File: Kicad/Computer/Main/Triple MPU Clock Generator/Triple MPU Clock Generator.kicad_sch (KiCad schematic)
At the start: 45 parts, among them IC1 AP7365-33WG-7, IC10 74LVC74APW,118, IC11 74LVC157APW,118, IC12 74LVC1G08GV,125, IC13 74LVC14APW,118, IC2 74LVC74APW,118, IC3 74LVC74APW,118, IC4 74LVC74APW,118, IC5 74LVC74APW,118, IC6 74LVC74APW,118, IC7 74LVC157APW,118, IC8 DS1813R-10+T&R, IC9 74LVC125APW-Q100J, J1 Conn_02x32_Counter_Clockwise, J10 Pin_Header_01x32, J11 Pin_Header_01x32, J2 Conn_01x03_Socket, J3 Conn_01x03_Socket, J4 Conn_01x03_Socket, J5 Conn_01x03_Socket, J6 Conn_01x03_Socket, J7 Conn_01x03_Socket, J8 Conn_01x03_Socket, J9 Conn_01x03_Socket

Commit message: Re-worked Dual Clock Generator.
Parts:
- removed IC9: 74LVC125APW-Q100J, SOP65P640X110-14N, symbol Nexperia:74LVC125APW-Q100J
- removed J2, J3, J4, J5, J6, J7, J8, J9: Conn_01x03_Socket, Connector_PinSocket_2.54mm:PinSocket_1x03_P2.54mm_Vertical, symbol Connector:Conn_01x03_Socket
- removed NT1: NetTie_2, NetTie:NetTie-2_SMD_Pad0.5mm, symbol Device:NetTie_2
- removed R1: 4.7KΩ, SamacSys_Parts:R_0805, symbol HCP65:R_0805
- removed RN1: CAY16-471J4LF, CAY16-J4, symbol Bourns:CAY16-471J4LF
- removed RN2: CAY16-151J4LF, SamacSys_Parts:CAY16-J4, symbol Bourns:CAY16-151J4LF
- removed S1: NDS-04-V, NDS04V, symbol Apem:NDS-04-V
- added CN1, CN2, CN3, CN4, CN5, CN6: CA0612KRX7R9BB100, SamacSys_Parts:CA0612KRX7R9BB100, symbol Yageo:CA0612KRX7R9BB100
- added J4, J5: Conn_01x04_Socket, Connector_PinSocket_2.54mm:PinSocket_1x04_P2.54mm_Vertical, symbol Connector:Conn_01x04_Socket
- added RN1, RN6, RN7, RN8, RN9: CAY16-200J4LF, CAY-16-F4, symbol Bourns:CAY16-200J4LF
- added RN3: CAY16-100J4LF, CAY-16-F4, symbol Bourns:CAY16-100J4LF
- R2: value 3.3KΩ -> 4.7KΩ
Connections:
- net 3.3V: now also J5.1 (Pin_1)
- net CK_{0}: now also RN8.1 (R1); no longer IC11.2 (1I0), IC4.12 (2D)
- net CK_{1}: now also RN9.1 (R1); no longer IC11.3 (1I1), IC5.12 (2D)
- net CK_{2}: now also RN8.2 (R2); no longer IC11.5 (2I0), IC6.12 (2D)
- net CK_{3}: now also RN9.2 (R2); no longer IC10.12 (2D), IC11.6 (2I1)
- net CK_{4}: now also RN8.3 (R3); no longer IC11.11 (3I0), IC2.12 (2D)
- net CK_{5}: now also RN9.3 (R3); no longer IC11.10 (3I1), IC3.12 (2D)
- net CLK: now also IC13.9 (4A), J5.3 (Pin_3); no longer IC12.2 (A)
- net GND: now also CN1.5, CN1.6, CN1.7, CN1.8, CN2.5, CN2.6, CN2.7, CN2.8, CN3.5, CN3.6, CN3.7, CN3.8, CN4.5, CN4.6, CN4.7, CN4.8, CN5.5, CN5.6, CN5.7, CN5.8, CN6.5, CN6.6, CN6.7, CN6.8, J4.3 (Pin_3); no longer IC13.13 (6A), IC13.9 (4A)
- net MA_{0}: now also RN6.2 (R2); no longer IC4.2 (1D), IC7.2 (1I0)
- net MA_{1}: now also RN7.2 (R2); no longer IC5.2 (1D), IC7.3 (1I1)
- net MA_{2}: now also RN6.3 (R3); no longer IC6.2 (1D), IC7.5 (2I0)
- net MA_{3}: now also RN7.3 (R3); no longer IC10.2 (1D), IC7.6 (2I1)
- net MA_{4}: now also RN6.4 (R4); no longer IC2.2 (1D), IC7.11 (3I0)
- net MA_{5}: now also RN7.4 (R4); no longer IC3.2 (1D), IC7.10 (3I1)
- net Reset: now also RN7.1 (R1); no longer IC13.3 (2A)
- net ~{Q}_{0}: now also RN8.4 (R4); no longer J1.11 (Pin_11)
- net ~{Q}_{1}: now also RN9.4 (R4); no longer J1.54 (Pin_54)
- net ~{Q}_{2}: now also RN1.4 (R4); no longer J1.44 (Pin_44)
- net ~{Reset}_{OUT}: now also IC13.12 (6Y)
- net ~{Y0}: now also RN1.1 (R1); no longer J1.13 (Pin_13)
- net ~{Y1}: now also RN1.2 (R2); no longer J1.52 (Pin_52)
- net ~{Y2}: now also RN1.3 (R3); no longer J1.46 (Pin_46)
- net ~{CLK}: now reaches IC13.8 (4Y)
- net ~{CLK}: now also RN3.2 (R2)
- net !(~{RST}⋅CLK) renamed !(R⋅CLK)_{s}
- net !(R⋅CLK)_{s}: now also CN1.3, RN3.6 (R3); no longer IC13.6 (3Y)
- net ~{RST} renamed ~{Reset}_{2s}
- net ~{Reset}_{2s}: now also IC13.13 (6A), CN2.1, J4.1 (Pin_1), RN6.8 (R1); no longer IC13.4 (2Y)
- net ~{RST}⋅CLK renamed R⋅CLK_{s}
- net R⋅CLK_{s}: now also CN1.4, RN3.5 (R4); no longer IC12.4 (Y)
- new net: CN1.1, RN3.8 (R1)
- new net !(R⋅CLK): IC13.6 (3Y), RN3.3 (R3)
- new net CK_{0s}: CN4.1, IC11.2 (1I0), IC4.12 (2D), RN8.8 (R1)
- new net CK_{1s}: CN5.1, IC11.3 (1I1), IC5.12 (2D), RN9.8 (R1)
- new net CK_{2s}: CN4.2, IC11.5 (2I0), IC6.12 (2D), RN8.7 (R2)
- new net CK_{3s}: CN5.2, IC10.12 (2D), IC11.6 (2I1), RN9.7 (R2)
- new net CK_{4s}: CN4.3, IC11.11 (3I0), IC2.12 (2D), RN8.6 (R3)
- new net CK_{5s}: CN5.3, IC11.10 (3I1), IC3.12 (2D), RN9.6 (R3)
- new net MA_{0s}: CN2.2, IC4.2 (1D), IC7.2 (1I0), RN6.7 (R2)
- new net MA_{1s}: CN3.2, IC5.2 (1D), IC7.3 (1I1), RN7.7 (R2)
- new net MA_{2s}: CN2.3, IC6.2 (1D), IC7.5 (2I0), RN6.6 (R3)
- new net MA_{3s}: CN3.3, IC10.2 (1D), IC7.6 (2I1), RN7.6 (R3)
- new net MA_{4s}: CN2.4, IC2.2 (1D), IC7.11 (3I0), RN6.5 (R4)
- new net MA_{5s}: CN3.4, IC3.2 (1D), IC7.10 (3I1), RN7.5 (R4)
- new net Reset_{s}: CN3.1, IC13.3 (2A), RN7.8 (R1)
- new net R⋅CLK: IC12.4 (Y), RN3.4 (R4)
- new net ~{CLK}_{s}: CN1.2, IC12.2 (A), RN3.7 (R2)
- new net ~{Q}_{0s}: CN4.4, J1.11 (Pin_11), RN8.5 (R4)
- new net ~{Q}_{1s}: CN5.4, J1.54 (Pin_54), RN9.5 (R4)
- new net ~{Q}_{2s}: CN6.4, J1.44 (Pin_44), RN1.5 (R4)
- new net ~{Reset}_{2}: IC13.4 (2Y), RN6.1 (R1)
- new net ~{Y0}_{s}: CN6.1, J1.13 (Pin_13), RN1.8 (R1)
- new net ~{Y1}_{s}: CN6.2, J1.52 (Pin_52), RN1.7 (R2)
- new net ~{Y2}_{s}: CN6.3, J1.46 (Pin_46), RN1.6 (R3)
- no-connect marks 69 -> 64

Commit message: Moved clock generator pins.
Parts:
- removed J1: Conn_02x32_Counter_Clockwise, SamacSys_Parts:DIP-64_Board_W22.86mm, symbol Connector_Generic:Conn_02x32_Counter_Clockwise
- added CN7, CN8: CA0612KRX7R9BB100, SamacSys_Parts:CA0612KRX7R9BB100, symbol Yageo:CA0612KRX7R9BB100
- added J2: Conn_02x32_Counter_Clockwise, SamacSys_Parts:DIP-64_Board_W22.86mm, symbol Connector_Generic:Conn_02x32_Counter_Clockwise
- added RN2, RN4: CAY16-200J4LF, CAY-16-F4, symbol Bourns:CAY16-200J4LF
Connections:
- net 3.3V: now also J5.2 (Pin_2), J2.61 (Pin_61); no longer J5.1 (Pin_1)
- net 5V: now also J4.1 (Pin_1), J2.3 (Pin_3), J2.35 (Pin_35)
- net CLK: now also J5.4 (Pin_4), J2.59 (Pin_59); no longer J5.3 (Pin_3)
- net GND: now also J4.4 (Pin_4), CN7.6, CN7.7, CN7.8, CN8.6, CN8.7, CN8.8, J2.10 (Pin_10), J2.23 (Pin_23), J2.42 (Pin_42), J2.55 (Pin_55), J2.6 (Pin_6); no longer CN1.8, CN3.8, IC13.11 (5A), J4.3 (Pin_3)
- net Reset: now also IC13.3 (2A); no longer RN7.1 (R1)
- net R⋅CLK: now also IC13.5 (3A)
- net R⋅CLK_{s}: no longer IC13.5 (3A)
- net ~{Q}_{0}: now also CN8.1, J2.11 (Pin_11), RN4.4 (R4); no longer IC11.4 (1Y)
- net ~{Q}_{1}: now also CN8.2, J2.14 (Pin_14), RN4.3 (R3); no longer IC11.7 (2Y)
- net ~{Q}_{2}: now also CN8.3, J2.17 (Pin_17), RN4.2 (R2); no longer IC11.9 (3Y)
- net ~{Reset}: now also J2.13 (Pin_13)
- net ~{Reset}_{2s}: now also IC13.11 (5A), J4.2 (Pin_2), J2.4 (Pin_4); no longer IC13.13 (6A), J4.1 (Pin_1)
- net ~{Reset}_{OUT}: now also J2.9 (Pin_9)
- net ~{Y0}: now also CN7.1, J2.12 (Pin_12), RN2.4 (R4); no longer IC7.4 (1Y)
- net ~{Y1}: now also CN7.2, J2.15 (Pin_15), RN2.3 (R3); no longer IC7.7 (2Y)
- net ~{Y2}: now also CN7.3, J2.18 (Pin_18), RN2.2 (R2); no longer IC7.9 (3Y)
- net Reset_{2}: now reaches IC13.10 (5Y)
- net Reset_{2}: now also IC13.13 (6A)
- net Reset_{s}: no longer names the net of CN3.1, RN7.8 (R1)
- net Reset_{s}: no longer IC13.3 (2A)
- new net: IC11.4 (1Y), RN4.5 (R4)
- new net: IC11.7 (2Y), RN4.6 (R3)
- new net: IC11.9 (3Y), RN4.7 (R2)
- new net: CN7.4, RN2.1 (R1)
- new net: IC7.4 (1Y), RN2.5 (R4)
- new net: IC7.7 (2Y), RN2.6 (R3)
- new net: IC7.9 (3Y), RN2.7 (R2)
- new net: CN8.4, RN4.1 (R1)
- new net ~{Q}_{3}: J2.20 (Pin_20)
- new net ~{Y3}: J2.21 (Pin_21)
- no-connect marks 64 -> 72
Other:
- note added: "(CLK_{0})"
- note added: "(CLK_{1})"
- note added: "(CLK_{2})"
- note added: "(CLK_{3})"
- note added: "(Main Access_{0})"
- note added: "(Main Access_{1})"
- note added: "(Main Access_{2})"
- note added: "(Main Access_{3})"
- note added: "(~{Reset} CLK)"
- note added: "(~{Reset} Switch)"
- moved on the sheet: IC8, J4, J5, R2, S2

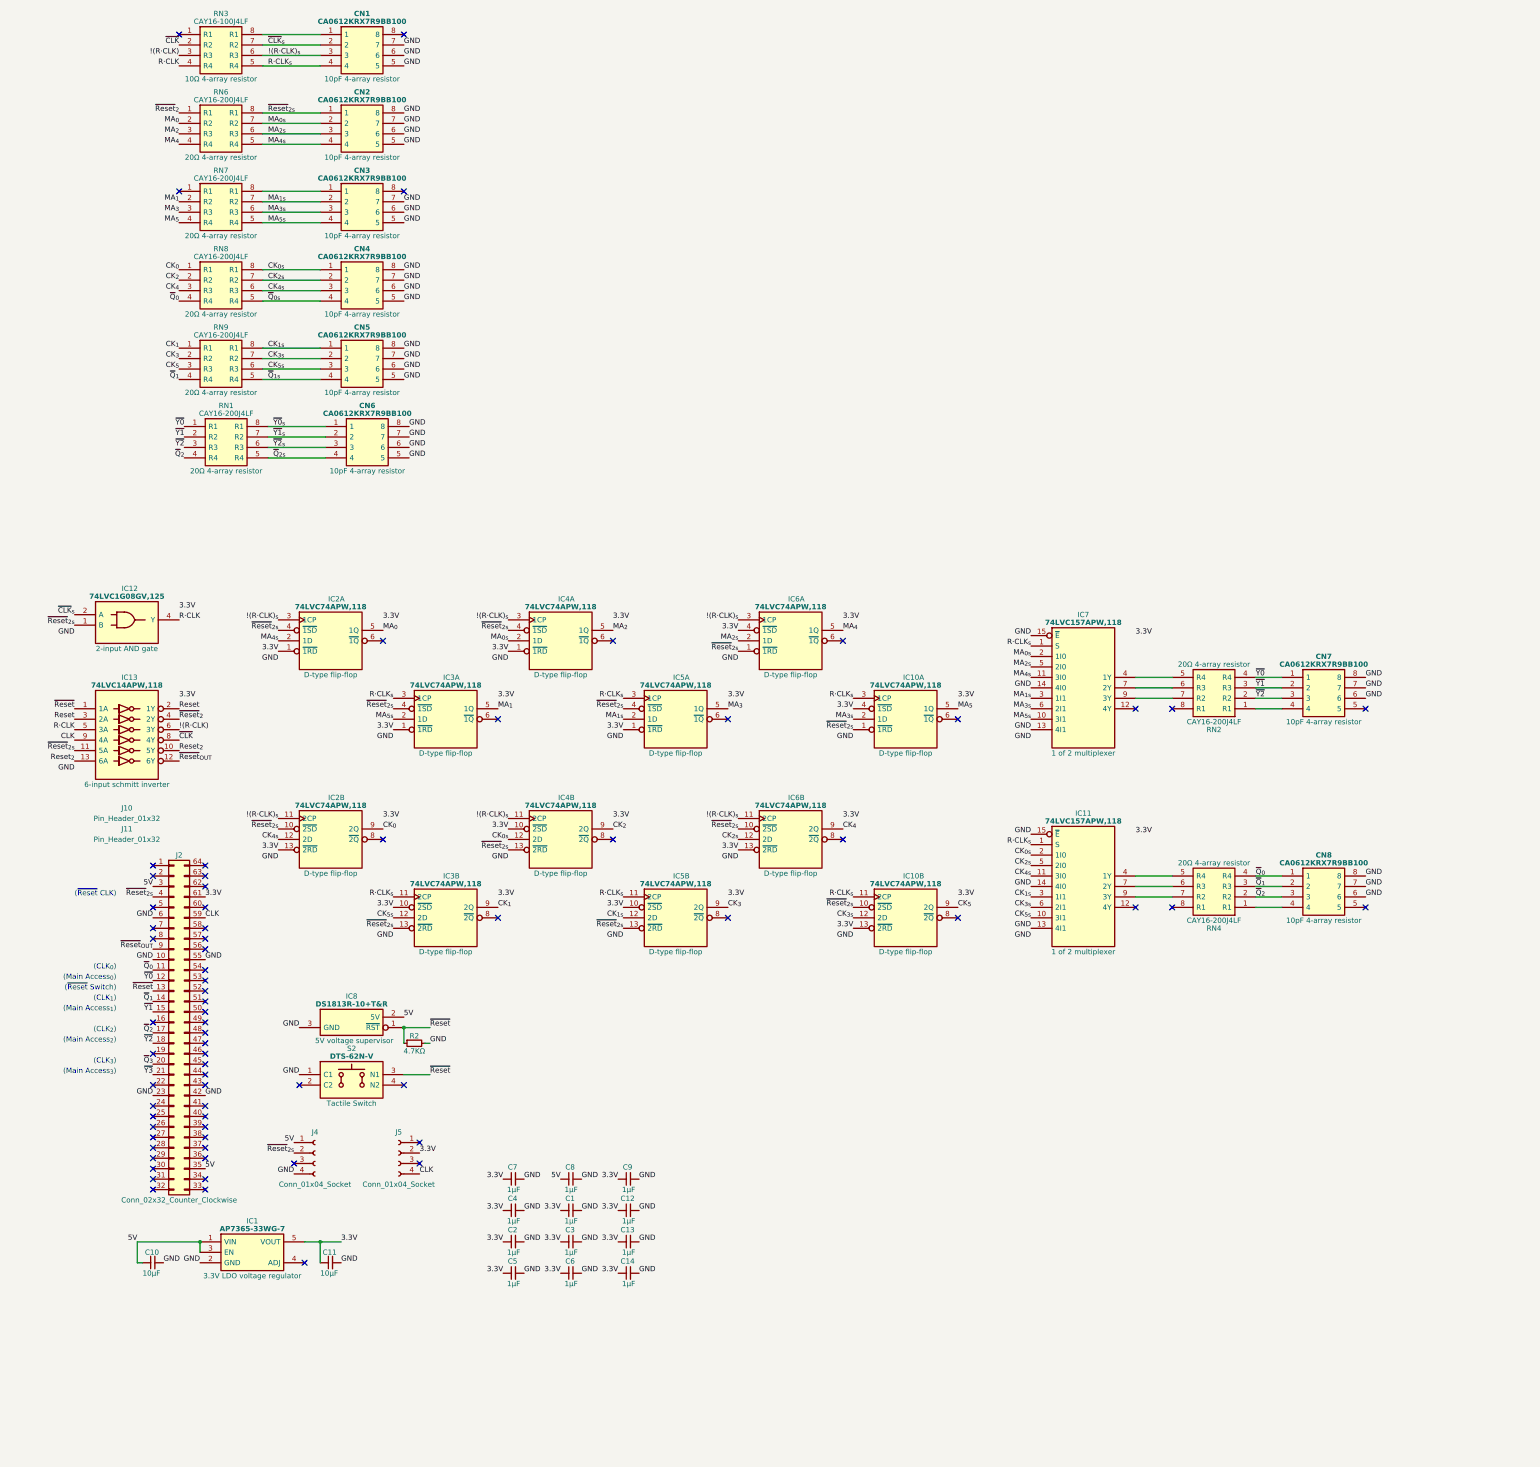
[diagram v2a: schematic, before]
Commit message: Routed Triple MPU Clock board.
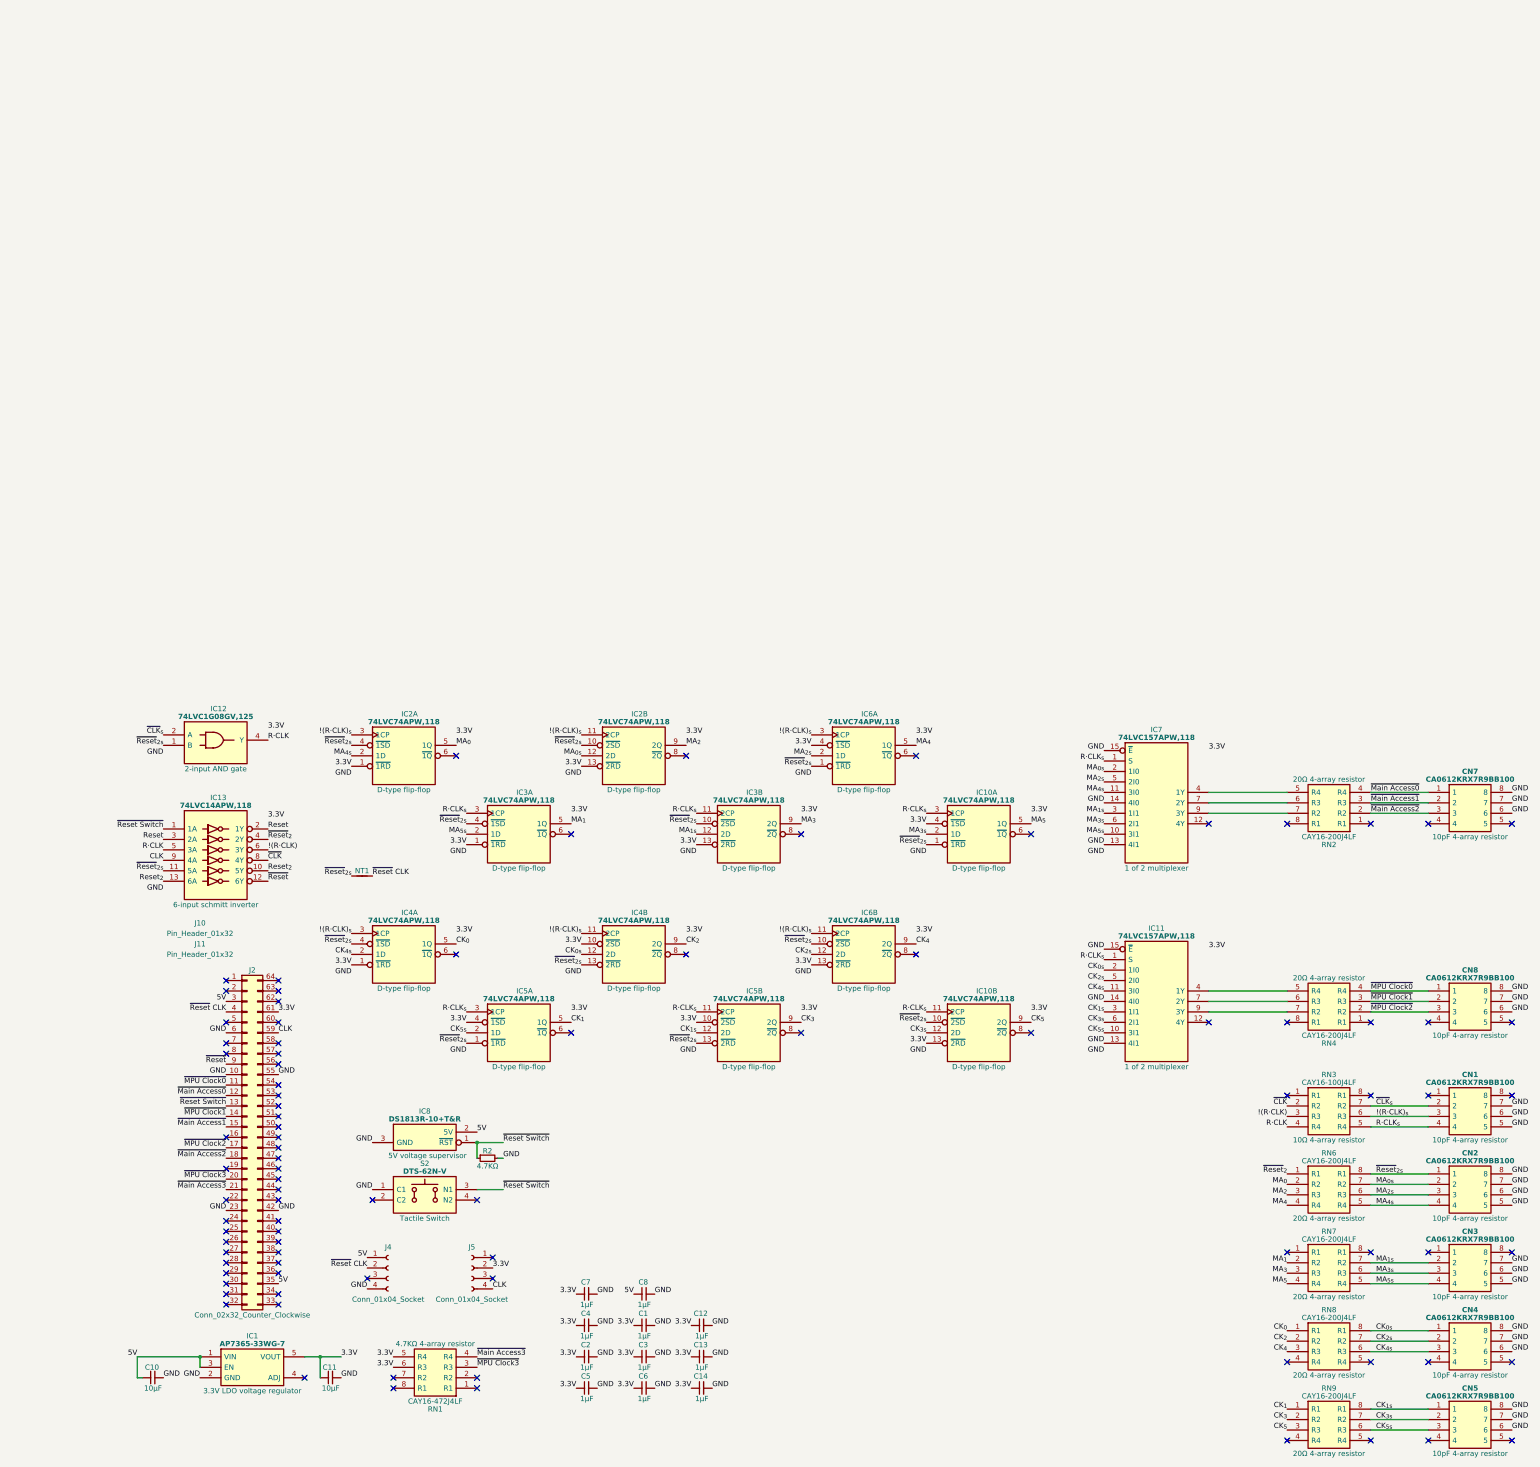
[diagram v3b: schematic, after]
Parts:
- removed C9: 1μF, SamacSys_Parts:C_0805, symbol HCP65:C_0805
- removed CN6: CA0612KRX7R9BB100, SamacSys_Parts:CA0612KRX7R9BB100, symbol Yageo:CA0612KRX7R9BB100
- removed RN1: CAY16-200J4LF, CAY-16-F4, symbol Bourns:CAY16-200J4LF
- added NT1: NetTie, NetTie:NetTie-2_SMD_Pad0.5mm, symbol HCP65:NetTie
- added RN1: CAY16-472J4LF, SamacSys_Parts:CAY16-F4, symbol Bourns:CAY16-472J4LF
- RN2, RN3, RN4, RN6, RN7, RN8, RN9: footprint CAY-16-F4 -> SamacSys_Parts:CAY16-F4
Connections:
- net ~{Reset}_{OUT} is gone; now on net ~{Reset}: IC13.12 (6Y), J2.9 (Pin_9)
- net 3.3V: now also IC3.13 (~{2RD}), IC5.4 (~{1SD}), RN1.5 (R4), RN1.6 (R3); no longer IC3.10 (~{2SD}), IC5.1 (~{1RD})
- net CK_{0}: now also IC4.5 (1Q); no longer IC2.9 (2Q)
- net CK_{1}: now also IC5.5 (1Q); no longer IC3.9 (2Q)
- net CK_{4s}: now also IC4.2 (1D); no longer IC2.12 (2D)
- net CK_{5s}: now also IC5.2 (1D); no longer IC3.12 (2D)
- net GND: no longer CN4.5, CN5.5
- net MA_{0s}: now also IC2.12 (2D); no longer IC4.2 (1D)
- net MA_{1s}: now also IC3.12 (2D); no longer IC5.2 (1D)
- net MA_{2}: now also IC2.9 (2Q); no longer IC4.5 (1Q)
- net MA_{3}: now also IC3.9 (2Q); no longer IC5.5 (1Q)
- net ~{Reset}: no longer IC13.1 (1A), IC8.1 (~{RST}), J2.13 (Pin_13), R2.1, S2.3 (N1)
- net ~{Reset}_{2s}: now also IC3.10 (~{2SD}), IC5.1 (~{1RD}), NT1.1; no longer IC3.13 (~{2RD}), IC5.4 (~{1SD}), J2.4 (Pin_4), J4.2 (Pin_2)
- net at CN1.1: no longer RN3.8 (R1)
- net at RN2.1 (R1): no longer CN7.4
- net at RN4.1 (R1): no longer CN8.4
- net at CN3.1: no longer RN7.8 (R1)
- net ~{Q}_{0s}: no longer names the net of RN8.5 (R4)
- net ~{Q}_{0s}: no longer CN4.4
- net ~{Q}_{0} renamed ~{MPU Clock0}
- net ~{MPU Clock0}: no longer RN8.4 (R4)
- net ~{Q}_{1s}: no longer names the net of CN5.4
- net ~{Q}_{1s}: no longer RN9.5 (R4)
- net ~{Q}_{1} renamed ~{MPU Clock1}
- net ~{MPU Clock1}: no longer RN9.4 (R4)
- net ~{Q}_{2} renamed ~{MPU Clock2}
- net ~{Q}_{3} renamed ~{MPU Clock3}
- net ~{MPU Clock3}: now also RN1.3 (R3)
- net ~{Y0} renamed ~{Main Access0}
- net ~{Y1} renamed ~{Main Access1}
- net ~{Y2} renamed ~{Main Access2}
- net ~{Y3} renamed ~{Main Access3}
- net ~{Main Access3}: now also RN1.4 (R4)
- new net ~{Reset Switch}: IC13.1 (1A), IC8.1 (~{RST}), J2.13 (Pin_13), R2.1, S2.3 (N1)
- new net ~{Reset} CLK: J2.4 (Pin_4), J4.2 (Pin_2), NT1.2
- no-connect marks 72 -> 92
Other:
- note removed: "(CLK_{0})"
- note removed: "(CLK_{1})"
- note removed: "(CLK_{2})"
- note removed: "(CLK_{3})"
- note removed: "(Main Access_{0})"
- note removed: "(Main Access_{1})"
- note removed: "(Main Access_{2})"
- note removed: "(Main Access_{3})"
- note removed: "(~{Reset} CLK)"
- note removed: "(~{Reset} Switch)"
- moved on the sheet: C1, C10, C11, C12, C13, C14, C2, C3, C4, C5, C6, C7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

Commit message: Routed Quad MPU Clock board.
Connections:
- net 5V: now also R2.2
- net GND: no longer R2.2
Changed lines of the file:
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@@
     (effects (font (size 1.27 1.27)) (justify right bottom))
   )
-  (label "GND" (at 123.19 162.56 0) (fields_autoplaced)
+  (label "5V" (at 123.19 162.56 0) (fields_autoplaced)
     (effects (font (size 1.27 1.27)) (justify left bottom))
   )
